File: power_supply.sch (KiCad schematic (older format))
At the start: 37 parts, among them Q2 NPN, U2 MC34063, U3 MC34063, U4 BP5037

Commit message: Adding back library files in same repo.
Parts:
- removed AC_L1, AC_N1, CONN2: CONN_1, symbol CONN_1
- removed C10: C, symbol C
- removed C7: CAPAPOL, symbol CAPAPOL
- removed CONN1: AMP_RELAY_1, symbol CONN_1
- removed D1: DIODE, symbol DIODE
- removed F1: FUSE, symbol FUSE
- removed L1: INDUCTOR, symbol INDUCTOR
- removed R7: R, symbol R
- removed U4: BP5037, MODULE, symbol BP5037
- removed VR1: VR, symbol VR
- added K1: G5LA-1, symbol G5LA-1
- added P0: CONN_4, symbol CONN_4
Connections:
- net labels added: AMP_PWR, AMP_RELAY_COIL, HT
- wire segments 48 -> 42
- no-connect marks 0 -> 1
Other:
- moved on the sheet: R12

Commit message: Changing dual fet module.
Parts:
- removed C11, C12, C13, C14, C5, C6, C8, C9: C, symbol C
- removed D2, D3: ZENER, symbol ZENER
- removed D4: DIODE, symbol DIODE
- removed K1: G5LA-1, symbol G5LA-1
- removed L2, L3, L4, L5: INDUCTOR, symbol INDUCTOR
- removed Q2: NPN, symbol NPN
- removed R10, R11, R12, R5, R6, R8, R9: R, symbol R
- removed U2, U3: MC34063, symbol MC34063
- added U3: DMP2066LSD, MODULE, symbol DMP2066LSD
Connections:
- net labels removed: +12V, -5V, AMP_PWR, HT
- wire segments 42 -> 17
- no-connect marks 1 -> 0

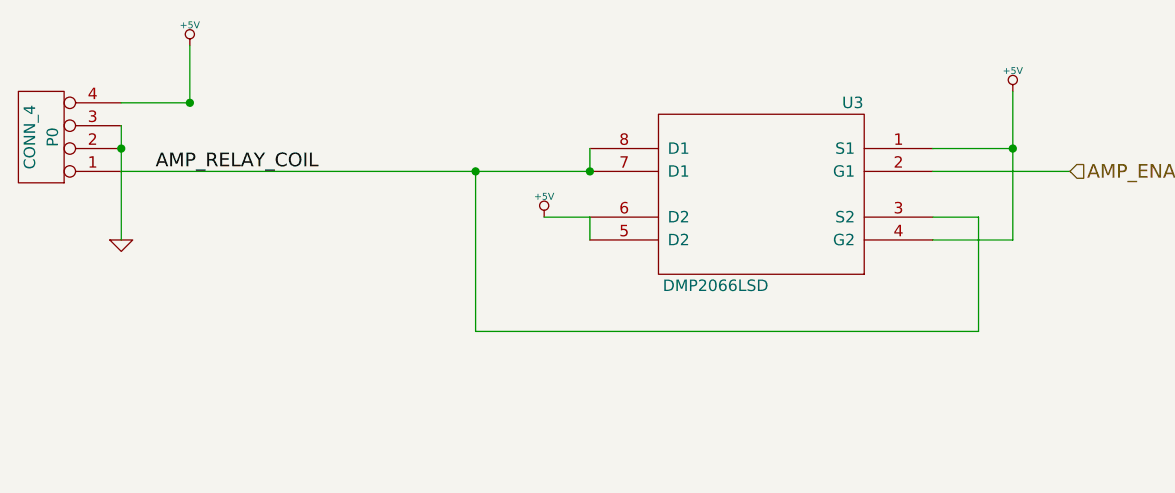
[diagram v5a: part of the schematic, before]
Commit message: Removing reset circuit, finishing audio circuit.
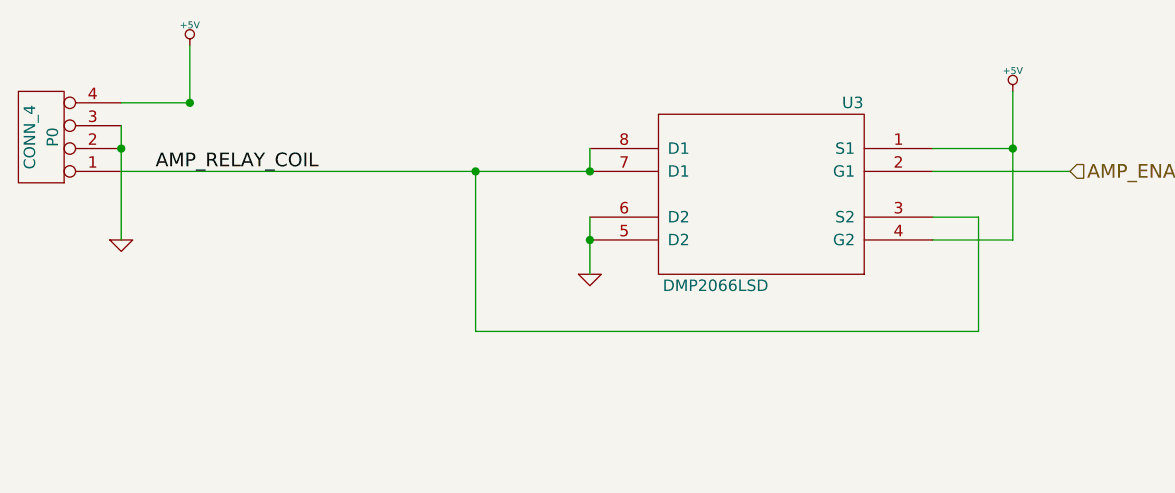
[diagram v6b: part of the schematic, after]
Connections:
- wire segments 17 -> 16
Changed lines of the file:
@@
-EESchema Schematic File Version 2  date 8/1/2012 10:20:13 AM
+EESchema Schematic File Version 2  date 8/1/2012 4:30:13 PM
 LIBS:atmel
 LIBS:device
@@
 Comment4 ""
 $EndDescr
+$Comp
+L GND #PWR034
+U 1 1 50195E98
+P 4350 1950
+F 0 "#PWR034" H 4350 1950 30  0001 C CNN
+F 1 "GND" H 4350 1880 30  0001 C CNN
+	1    4350 1950
+	1    0    0    -1
+$EndComp
+Connection ~ 4350 1800
 Wire Wire Line
-	4150 1700 4350 1700
+	4350 1950 4350 1700
 Wire Wire Line
-	3850 2200 6050 2200
-Connection ~ 3850 1500
+	6050 1700 6050 2200
 Wire Wire Line
-	3850 2200 3850 1500
+	6050 1700 5850 1700
+Connection ~ 6200 1400
 Wire Wire Line
-	6200 1150 6200 1800
+	2300 1200 2600 1200
 Wire Wire Line
-	6200 1800 5850 1800
+	5850 1500 6450 1500
+Connection ~ 4350 1500
 Wire Wire Line
-	4350 1400 4350 1500
+	2600 1200 2600 950
 Wire Wire Line
-	6200 1400 5850 1400
-Connection ~ 2300 1400
-Connection ~ 2600 1200
+	6950 6500 6950 6450
 Wire Wire Line
-	4350 1500 2300 1500
+	4200 3900 4200 4000
 Wire Wire Line
 	2300 1300 2300 1800
 Wire Wire Line
-	4200 3900 4200 4000
+	2300 1500 4350 1500
+Connection ~ 2600 1200
+Connection ~ 2300 1400
 Wire Wire Line
-	6950 6500 6950 6450
+	6200 1400 5850 1400
 Wire Wire Line
-	2600 950  2600 1200
-Connection ~ 4350 1500
+	4350 1500 4350 1400
 Wire Wire Line
-	5850 1500 6450 1500
+	5850 1800 6200 1800
 Wire Wire Line
-	2600 1200 2300 1200
-Connection ~ 6200 1400
+	6200 1800 6200 1150
 Wire Wire Line
-	4350 1700 4350 1800
+	3850 1500 3850 2200
+Connection ~ 3850 1500
 Wire Wire Line
-	5850 1700 6050 1700
-Wire Wire Line
-	6050 1700 6050 2200
+	3850 2200 6050 2200
 $Comp
-L +5V #PWR040
-U 1 1 50189E8B
-P 4150 1700
-F 0 "#PWR040" H 4150 1790 20  0001 C CNN
-F 1 "+5V" H 4150 1790 30  0000 C CNN
-	1    4150 1700
-	-1   0    0    -1
-$EndComp
-$Comp
-L +5V #PWR041
+L +5V #PWR035
 U 1 1 50189DC4
 P 6200 1150
-F 0 "#PWR041" H 6200 1240 20  0001 C CNN
+F 0 "#PWR035" H 6200 1240 20  0001 C CNN
 F 1 "+5V" H 6200 1240 30  0000 C CNN
 	1    6200 1150
@@
 $EndComp
 $Comp
-L +5V #PWR042
+L +5V #PWR036
 U 1 1 50189DBE
 P 2600 950
-F 0 "#PWR042" H 2600 1040 20  0001 C CNN
+F 0 "#PWR036" H 2600 1040 20  0001 C CNN
 F 1 "+5V" H 2600 1040 30  0000 C CNN
 	1    2600 950
@@
 AMP_RELAY_COIL
 $Comp
-L GND #PWR043
+L GND #PWR037
 U 1 1 50078FA5
 P 2300 1800
-F 0 "#PWR043" H 2300 1800 30  0001 C CNN
+F 0 "#PWR037" H 2300 1800 30  0001 C CNN
 F 1 "GND" H 2300 1730 30  0001 C CNN
 	1    2300 1800
@@
 $EndComp
 $Comp
-L GND #PWR044
+L GND #PWR038
 U 1 1 4F9344B8
 P 4200 4000
-F 0 "#PWR044" H 4200 4000 30  0001 C CNN
+F 0 "#PWR038" H 4200 4000 30  0001 C CNN
 F 1 "GND" H 4200 3930 30  0001 C CNN
 	1    4200 4000

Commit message: Final touches on a rev0.0 candidate.
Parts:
- added C1, C2: 15u, symbol C
- added U1: MAX660, MODULE, symbol MAX660
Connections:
- net labels added: -5V
- wire segments 16 -> 22
- no-connect marks 0 -> 2
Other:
- note added: "Second FET in this package is just being used as a diode."
- moved on the sheet: P0, U3
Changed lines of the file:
@@
-EESchema Schematic File Version 2  date 8/1/2012 4:30:13 PM
+EESchema Schematic File Version 2  date 8/1/2012 10:55:27 PM
 LIBS:atmel
 LIBS:device
@@
 LIBS:RC4580
 LIBS:DMP2066LSD
+LIBS:MAX660
 LIBS:kenwood-cache
 EELAYER 25  0
@@
 Sheet 3 3
 Title ""
-Date "1 aug 2012"
+Date "2 aug 2012"
 Rev ""
 Comp ""
@@
 Comment4 ""
 $EndDescr
+Text Notes 5650 3950 0    60   ~ 0
+Second FET in this package is just being used as a diode.
+NoConn ~ 2800 5100
+Wire Wire Line
+	3550 4300 2800 4300
+Wire Wire Line
+	2800 4300 2800 4800
+Wire Wire Line
+	4300 4950 4800 4950
+Wire Wire Line
+	4450 3700 6650 3700
+Connection ~ 4450 3000
+Wire Wire Line
+	4450 3700 4450 3000
+Wire Wire Line
+	6800 2650 6800 3300
+Wire Wire Line
+	6800 3300 6450 3300
+Wire Wire Line
+	4950 2900 4950 3000
+Wire Wire Line
+	6800 2900 6450 2900
+Connection ~ 2900 2900
+Connection ~ 3200 2700
+Wire Wire Line
+	4950 3000 2900 3000
+Wire Wire Line
+	2900 2800 2900 3300
+Wire Wire Line
+	3200 2450 3200 2700
+Connection ~ 4950 3000
+Wire Wire Line
+	6450 3000 7050 3000
+Wire Wire Line
+	3200 2700 2900 2700
+Connection ~ 6800 2900
+Wire Wire Line
+	6450 3200 6650 3200
+Wire Wire Line
+	6650 3200 6650 3700
+Wire Wire Line
+	4950 3450 4950 3200
+Connection ~ 4950 3300
+Wire Wire Line
+	4300 4800 4500 4800
+Wire Wire Line
+	4500 4800 4500 4550
+Wire Wire Line
+	4500 4550 4800 4550
+Wire Wire Line
+	4300 5100 5650 5100
+Wire Wire Line
+	5650 5100 5650 4950
+Connection ~ 4800 5100
+NoConn ~ 2800 4950
+$Comp
+L +5V #PWR033
+U 1 1 5019EAE9
+P 3550 4300
+F 0 "#PWR033" H 3550 4390 20  0001 C CNN
+F 1 "+5V" H 3550 4390 30  0000 C CNN
+	1    3550 4300
+	1    0    0    -1
+$EndComp
 $Comp
 L GND #PWR034
+U 1 1 5019EADB
+P 3550 5600
+F 0 "#PWR034" H 3550 5600 30  0001 C CNN
+F 1 "GND" H 3550 5530 30  0001 C CNN
+	1    3550 5600
+	1    0    0    -1
+$EndComp
+$Comp
+L GND #PWR035
+U 1 1 5019EAD5
+P 4800 5500
+F 0 "#PWR035" H 4800 5500 30  0001 C CNN
+F 1 "GND" H 4800 5430 30  0001 C CNN
+	1    4800 5500
+	1    0    0    -1
+$EndComp
+$Comp
+L -5V #PWR036
+U 1 1 5019EACF
+P 5650 4950
+F 0 "#PWR036" H 5650 5090 20  0001 C CNN
+F 1 "-5V" H 5650 5060 30  0000 C CNN
+	1    5650 4950
+	1    0    0    -1
+$EndComp
+$Comp
+L C C2
+U 1 1 5019EAB5
+P 4800 5300
+F 0 "C2" H 4850 5400 50  0000 L CNN
+F 1 "15u" H 4850 5200 50  0000 L CNN
+	1    4800 5300
+	1    0    0    -1
+$EndComp
+$Comp
+L C C1
+U 1 1 5019EAA1
+P 4800 4750
+F 0 "C1" H 4850 4850 50  0000 L CNN
+F 1 "15u" H 4850 4650 50  0000 L CNN
+	1    4800 4750
+	1    0    0    -1
+$EndComp
+$Comp
+L MAX660 U1
+U 1 1 5019E9C9
+P 3550 4950
+F 0 "U1" H 3550 4850 50  0000 C CNN
+F 1 "MAX660" H 3550 5050 50  0000 C CNN
+F 2 "MODULE" H 3550 4950 50  0001 C CNN
+F 3 "DOCUMENTATION" H 3550 4950 50  0001 C CNN
+	1    3550 4950
+	1    0    0    -1
+$EndComp
+$Comp
+L GND #PWR037
 U 1 1 50195E98
-P 4350 1950
-F 0 "#PWR034" H 4350 1950 30  0001 C CNN
-F 1 "GND" H 4350 1880 30  0001 C CNN
-	1    4350 1950
-	1    0    0    -1
-$EndComp
-Connection ~ 4350 1800
-Wire Wire Line
-	4350 1950 4350 1700
-Wire Wire Line
-	6050 1700 6050 2200
-Wire Wire Line
-	6050 1700 5850 1700
-Connection ~ 6200 1400
-Wire Wire Line
-	2300 1200 2600 1200
-Wire Wire Line
-	5850 1500 6450 1500
-Connection ~ 4350 1500
-Wire Wire Line
-	2600 1200 2600 950
-Wire Wire Line
-	6950 6500 6950 6450
-Wire Wire Line
-	4200 3900 4200 4000
-Wire Wire Line
-	2300 1300 2300 1800
-Wire Wire Line
-	2300 1500 4350 1500
-Connection ~ 2600 1200
-Connection ~ 2300 1400
-Wire Wire Line
-	6200 1400 5850 1400
-Wire Wire Line
-	4350 1500 4350 1400
-Wire Wire Line
-	5850 1800 6200 1800
-Wire Wire Line
-	6200 1800 6200 1150
-Wire Wire Line
-	3850 1500 3850 2200
-Connection ~ 3850 1500
-Wire Wire Line
-	3850 2200 6050 2200
-$Comp
-L +5V #PWR035
+P 4950 3450
+F 0 "#PWR037" H 4950 3450 30  0001 C CNN
+F 1 "GND" H 4950 3380 30  0001 C CNN
+	1    4950 3450
+	1    0    0    -1
+$EndComp
+$Comp
+L +5V #PWR038
 U 1 1 50189DC4
-P 6200 1150
-F 0 "#PWR035" H 6200 1240 20  0001 C CNN
-F 1 "+5V" H 6200 1240 30  0000 C CNN
-	1    6200 1150
+P 6800 2650
+F 0 "#PWR038" H 6800 2740 20  0001 C CNN
+F 1 "+5V" H 6800 2740 30  0000 C CNN
+	1    6800 2650
 	-1   0    0    -1
 $EndComp
 $Comp
-L +5V #PWR036
+L +5V #PWR039
 U 1 1 50189DBE
-P 2600 950
-F 0 "#PWR036" H 2600 1040 20  0001 C CNN
-F 1 "+5V" H 2600 1040 30  0000 C CNN
-	1    2600 950
+P 3200 2450
+F 0 "#PWR039" H 3200 2540 20  0001 C CNN
+F 1 "+5V" H 3200 2540 30  0000 C CNN
+	1    3200 2450
 	1    0    0    -1
 $EndComp
@@
 L DMP2066LSD U3
 U 1 1 50189D6F
-P 5100 1600
-F 0 "U3" H 4700 2000 50  0000 C CNN
-F 1 "DMP2066LSD" H 5300 1200 50  0000 C CNN
-F 2 "MODULE" H 4800 1200 50  0001 C CNN
-F 3 "DOCUMENTATION" H 5100 1300 50  0001 C CNN
-	1    5100 1600
+P 5700 3100
+F 0 "U3" H 5300 3500 50  0000 C CNN
+F 1 "DMP2066LSD" H 5900 2700 50  0000 C CNN
+F 2 "MODULE" H 5400 2700 50  0001 C CNN
+F 3 "DOCUMENTATION" H 5700 2800 50  0001 C CNN
+	1    5700 3100
 	-1   0    0    -1
 $EndComp
-Text Label 2450 1500 0    60   ~ 0
+Text Label 3050 3000 0    60   ~ 0
 AMP_RELAY_COIL
 $Comp
-L GND #PWR037
+L GND #PWR040
 U 1 1 50078FA5
-P 2300 1800
-F 0 "#PWR037" H 2300 1800 30  0001 C CNN
-F 1 "GND" H 2300 1730 30  0001 C CNN
-	1    2300 1800
+P 2900 3300
+F 0 "#PWR040" H 2900 3300 30  0001 C CNN
+F 1 "GND" H 2900 3230 30  0001 C CNN
+	1    2900 3300
 	1    0    0    -1
 $EndComp
@@
 L CONN_4 P0
 U 1 1 50076640
-P 1950 1350
-F 0 "P0" V 1900 1350 50  0000 C CNN
-F 1 "CONN_4" V 2000 1350 50  0000 C CNN
-	1    1950 1350
+P 2550 2850
+F 0 "P0" V 2500 2850 50  0000 C CNN
+F 1 "CONN_4" V 2600 2850 50  0000 C CNN
+	1    2550 2850
 	-1   0    0    1
 $EndComp
-$Comp
-L GND #PWR038
-U 1 1 4F9344B8
-P 4200 4000
-F 0 "#PWR038" H 4200 4000 30  0001 C CNN
-F 1 "GND" H 4200 3930 30  0001 C CNN
-	1    4200 4000
-	1    0    0    -1
-$EndComp
-Text HLabel 6450 1500 2    60   Input ~ 0
+Text HLabel 7050 3000 2    60   Input ~ 0
 AMP_ENABLE
 $EndSCHEMATC

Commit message: Final board as sent for fab.
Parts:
- added C10, C11: 150u, symbol CP1
- added C?: 0.33u, symbol C
- added F1: FUSE, symbol FUSE
- added U9: LM7805, symbol LM7805
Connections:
- net +5V: now also C10.1, U9.VO; no longer P0.4 (P4)
- net -5V: now also C11.2
- net GND: now also C10.2, C11.1, C?.2, U9.GND
- new net: F1.1, P0.4 (P4)
- new net: C?.1, F1.2, U9.VI
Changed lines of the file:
@@
-EESchema Schematic File Version 2  date 8/1/2012 10:55:27 PM
+EESchema Schematic File Version 2  date 8/3/2012 1:01:40 PM
 LIBS:atmel
 LIBS:device
@@
 Sheet 3 3
 Title ""
-Date "2 aug 2012"
+Date "3 aug 2012"
 Rev ""
 Comp ""
@@
 Comment4 ""
 $EndDescr
+Connection ~ 4100 1900
+Wire Wire Line
+	3900 1900 4400 1900
+Wire Wire Line
+	3400 1900 3150 1900
+Wire Wire Line
+	3150 1900 3150 2700
+Wire Wire Line
+	3150 2700 2900 2700
+Connection ~ 4800 5100
+Wire Wire Line
+	5650 4950 5650 5100
+Wire Wire Line
+	5650 5100 4300 5100
+Wire Wire Line
+	4800 4550 4500 4550
+Wire Wire Line
+	4500 4550 4500 4800
+Wire Wire Line
+	4500 4800 4300 4800
+Connection ~ 4950 3300
+Wire Wire Line
+	4950 3200 4950 3450
+Wire Wire Line
+	6650 3200 6650 3700
+Wire Wire Line
+	6650 3200 6450 3200
+Connection ~ 6800 2900
+Wire Wire Line
+	6450 3000 7050 3000
+Connection ~ 4950 3000
+Wire Wire Line
+	2900 3300 2900 2800
+Wire Wire Line
+	2900 3000 4950 3000
+Connection ~ 2900 2900
+Wire Wire Line
+	6450 2900 6800 2900
+Wire Wire Line
+	4950 3000 4950 2900
+Wire Wire Line
+	6450 3300 6800 3300
+Wire Wire Line
+	6800 3300 6800 2650
+Wire Wire Line
+	4450 3000 4450 3700
+Connection ~ 4450 3000
+Wire Wire Line
+	4450 3700 6650 3700
+Wire Wire Line
+	4300 4950 4800 4950
+Wire Wire Line
+	2800 4800 2800 4300
+Wire Wire Line
+	2800 4300 3550 4300
+Connection ~ 5350 5100
+Wire Wire Line
+	5900 1900 5200 1900
+Connection ~ 5450 1900
+$Comp
+L GND #PWR?
+U 1 1 501C03E7
+P 4100 2300
+F 0 "#PWR?" H 4100 2300 30  0001 C CNN
+F 1 "GND" H 4100 2230 30  0001 C CNN
+	1    4100 2300
+	1    0    0    -1
+$EndComp
+$Comp
+L C C?
+U 1 1 501C03D0
+P 4100 2100
+F 0 "C?" H 4150 2200 50  0000 L CNN
+F 1 "0.33u" H 4150 2000 50  0000 L CNN
+	1    4100 2100
+	1    0    0    -1
+$EndComp
+$Comp
+L GND #PWR037
+U 1 1 501C00FA
+P 4800 2200
+F 0 "#PWR037" H 4800 2200 30  0001 C CNN
+F 1 "GND" H 4800 2130 30  0001 C CNN
+	1    4800 2200
+	1    0    0    -1
+$EndComp
+$Comp
+L LM7805 U9
+U 1 1 501C00DD
+P 4800 1950
+F 0 "U9" H 4950 1754 60  0000 C CNN
+F 1 "LM7805" H 4800 2150 60  0000 C CNN
+F 4 "497-2957-5-ND" H 4800 1950 60  0001 C CNN "Digikey"
+	1    4800 1950
+	1    0    0    -1
+$EndComp
+$Comp
+L GND #PWR038
+U 1 1 501BED49
+P 5350 4700
+F 0 "#PWR038" H 5350 4700 30  0001 C CNN
+F 1 "GND" H 5350 4630 30  0001 C CNN
+	1    5350 4700
+	-1   0    0    1
+$EndComp
+$Comp
+L GND #PWR039
+U 1 1 501BED47
+P 5450 2300
+F 0 "#PWR039" H 5450 2300 30  0001 C CNN
+F 1 "GND" H 5450 2230 30  0001 C CNN
+	1    5450 2300
+	1    0    0    -1
+$EndComp
+$Comp
+L CP1 C10
+U 1 1 501BED37
+P 5450 2100
+F 0 "C10" H 5500 2200 50  0000 L CNN
+F 1 "150u" H 5500 2000 50  0000 L CNN
+F 4 "P5138-ND" H 5450 2100 60  0001 C CNN "Digikey"
+	1    5450 2100
+	1    0    0    -1
+$EndComp
+$Comp
+L CP1 C11
+U 1 1 501BED26
+P 5350 4900
+F 0 "C11" H 5400 5000 50  0000 L CNN
+F 1 "150u" H 5400 4800 50  0000 L CNN
+F 4 "P5138-ND" H 5350 4900 60  0001 C CNN "Digikey"
+	1    5350 4900
+	1    0    0    -1
+$EndComp
+$Comp
+L FUSE F1
+U 1 1 501BEAB5
+P 3650 1900
+F 0 "F1" H 3750 1950 40  0000 C CNN
+F 1 "FUSE" H 3550 1850 40  0000 C CNN
+F 4 "507-1482-1-ND" H 3650 1900 60  0001 C CNN "Digikey"
+	1    3650 1900
+	1    0    0    -1
+$EndComp
 Text Notes 5650 3950 0    60   ~ 0
 Second FET in this package is just being used as a diode.
 NoConn ~ 2800 5100
-Wire Wire Line
-	3550 4300 2800 4300
-Wire Wire Line
-	2800 4300 2800 4800
-Wire Wire Line
-	4300 4950 4800 4950
-Wire Wire Line
-	4450 3700 6650 3700
-Connection ~ 4450 3000
-Wire Wire Line
-	4450 3700 4450 3000
-Wire Wire Line
-	6800 2650 6800 3300
-Wire Wire Line
-	6800 3300 6450 3300
-Wire Wire Line
-	4950 2900 4950 3000
-Wire Wire Line
-	6800 2900 6450 2900
-Connection ~ 2900 2900
-Connection ~ 3200 2700
-Wire Wire Line
-	4950 3000 2900 3000
-Wire Wire Line
-	2900 2800 2900 3300
-Wire Wire Line
-	3200 2450 3200 2700
-Connection ~ 4950 3000
-Wire Wire Line
-	6450 3000 7050 3000
-Wire Wire Line
-	3200 2700 2900 2700
-Connection ~ 6800 2900
-Wire Wire Line
-	6450 3200 6650 3200
-Wire Wire Line
-	6650 3200 6650 3700
-Wire Wire Line
-	4950 3450 4950 3200
-Connection ~ 4950 3300
-Wire Wire Line
-	4300 4800 4500 4800
-Wire Wire Line
-	4500 4800 4500 4550
-Wire Wire Line
-	4500 4550 4800 4550
-Wire Wire Line
-	4300 5100 5650 5100
-Wire Wire Line
-	5650 5100 5650 4950
-Connection ~ 4800 5100
 NoConn ~ 2800 4950
 $Comp
-L +5V #PWR033
+L +5V #PWR040
 U 1 1 5019EAE9
 P 3550 4300
-F 0 "#PWR033" H 3550 4390 20  0001 C CNN
+F 0 "#PWR040" H 3550 4390 20  0001 C CNN
 F 1 "+5V" H 3550 4390 30  0000 C CNN
 	1    3550 4300
@@
 $EndComp
 $Comp
-L GND #PWR034
+L GND #PWR041
 U 1 1 5019EADB
 P 3550 5600
-F 0 "#PWR034" H 3550 5600 30  0001 C CNN
+F 0 "#PWR041" H 3550 5600 30  0001 C CNN
 F 1 "GND" H 3550 5530 30  0001 C CNN
 	1    3550 5600
@@
 $EndComp
 $Comp
-L GND #PWR035
+L GND #PWR042
 U 1 1 5019EAD5
 P 4800 5500
-F 0 "#PWR035" H 4800 5500 30  0001 C CNN
+F 0 "#PWR042" H 4800 5500 30  0001 C CNN
 F 1 "GND" H 4800 5430 30  0001 C CNN
 	1    4800 5500
@@
 $EndComp
 $Comp
-L -5V #PWR036
+L -5V #PWR043
 U 1 1 5019EACF
 P 5650 4950
-F 0 "#PWR036" H 5650 5090 20  0001 C CNN
+F 0 "#PWR043" H 5650 5090 20  0001 C CNN
 F 1 "-5V" H 5650 5060 30  0000 C CNN
 	1    5650 4950
@@
 $EndComp
 $Comp
-L GND #PWR037
+L GND #PWR044
 U 1 1 50195E98
 P 4950 3450
-F 0 "#PWR037" H 4950 3450 30  0001 C CNN
+F 0 "#PWR044" H 4950 3450 30  0001 C CNN
 F 1 "GND" H 4950 3380 30  0001 C CNN
 	1    4950 3450
@@
 $EndComp
 $Comp
-L +5V #PWR038
+L +5V #PWR045
 U 1 1 50189DC4
 P 6800 2650
-F 0 "#PWR038" H 6800 2740 20  0001 C CNN
+F 0 "#PWR045" H 6800 2740 20  0001 C CNN
 F 1 "+5V" H 6800 2740 30  0000 C CNN
 	1    6800 2650
@@
 $EndComp
 $Comp
-L +5V #PWR039
+L +5V #PWR046
 U 1 1 50189DBE
-P 3200 2450
-F 0 "#PWR039" H 3200 2540 20  0001 C CNN
-F 1 "+5V" H 3200 2540 30  0000 C CNN
-	1    3200 2450
-	1    0    0    -1
+P 5900 1900
+F 0 "#PWR046" H 5900 1990 20  0001 C CNN
+F 1 "+5V" H 5900 1990 30  0000 C CNN
+	1    5900 1900
+	0    1    1    0
 $EndComp
 $Comp
@@
 AMP_RELAY_COIL
 $Comp
-L GND #PWR040
+L GND #PWR047
 U 1 1 50078FA5
 P 2900 3300
-F 0 "#PWR040" H 2900 3300 30  0001 C CNN
+F 0 "#PWR047" H 2900 3300 30  0001 C CNN
 F 1 "GND" H 2900 3230 30  0001 C CNN
 	1    2900 3300
